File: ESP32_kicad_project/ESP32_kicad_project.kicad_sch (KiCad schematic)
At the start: 24 parts, among them J2 USB_C_Receptacle_USB2.0_16P, J3 Screw_Terminal_01x02, Q1 AO3401A, U1 TPS56339DDC

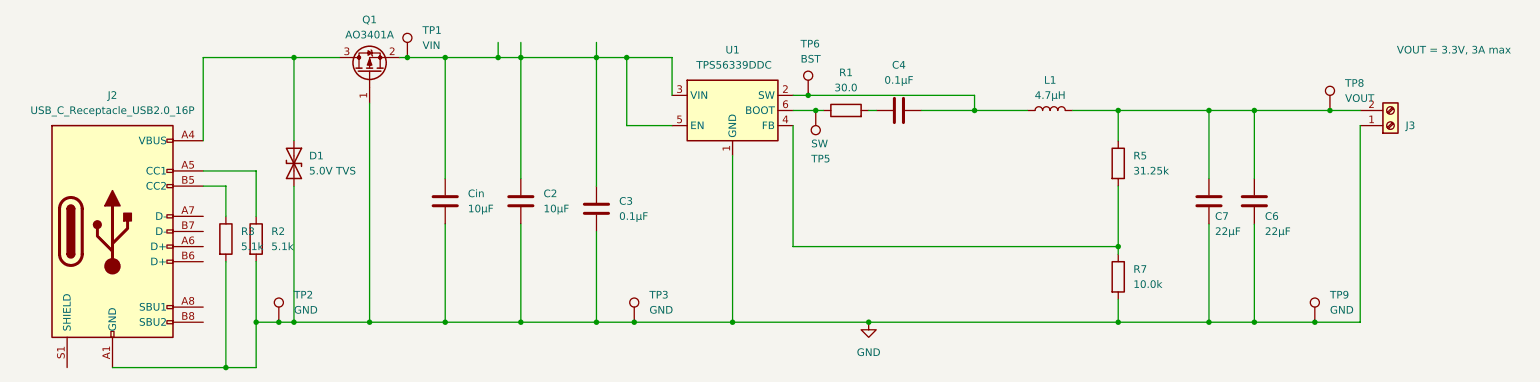
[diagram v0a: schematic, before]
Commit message: added fuse, fixed electrical rules checker errors
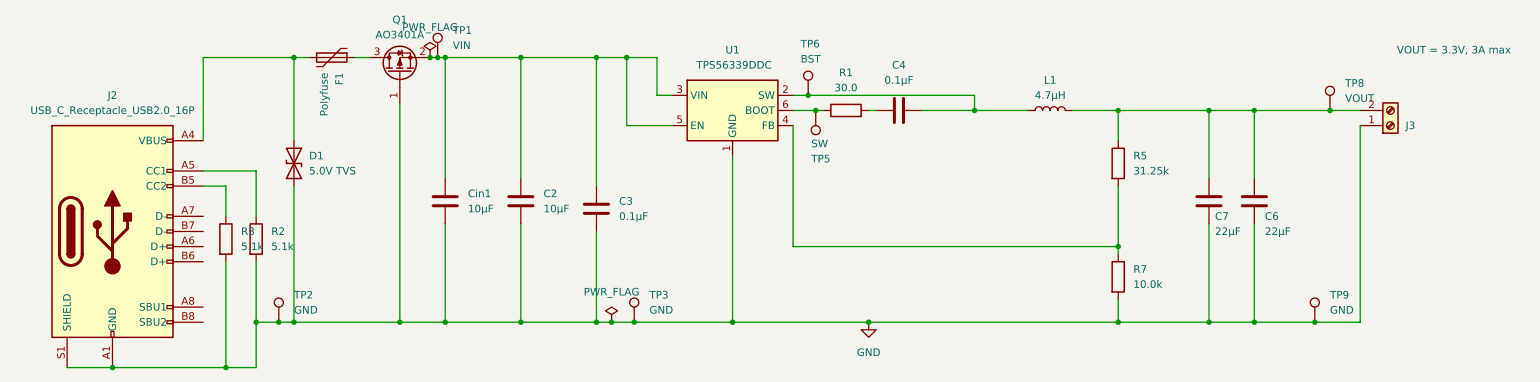
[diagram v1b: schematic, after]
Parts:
- added F1: Polyfuse, Fuse:Fuse_1206_3216Metric, symbol Device:Polyfuse
- D1: footprint Package_TO_SOT_SMD:SOD-323 -> Diode_SMD:D_SOD-323
- renumbered Cin to Cin1
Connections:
- net GND: now also J2.S1 (SHIELD)
- net at D1.1 (A1), J2.A4 (VBUS), J2.A9 (VBUS)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: now also F1.2; no longer Q1.3 (D)
- new net: F1.1, Q1.3 (D)
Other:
- moved on the sheet: Q1, TP1

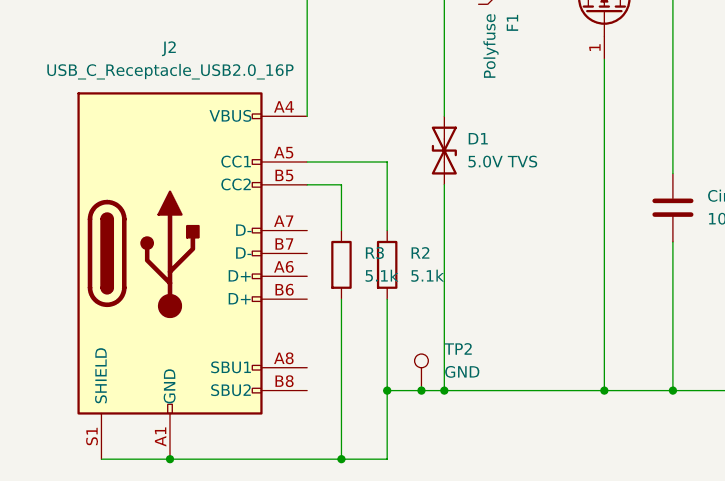
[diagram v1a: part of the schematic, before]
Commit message: created: inductor footprint, assigned it to L1, power unit
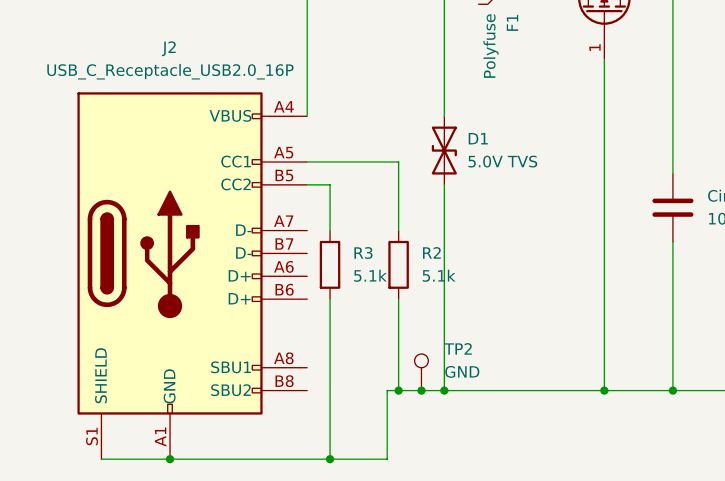
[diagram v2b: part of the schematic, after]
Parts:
- C2, Cin1: footprint (none) -> Capacitor_SMD:C_0805_2012Metric
- C3, C4: footprint (none) -> Capacitor_SMD:C_0603_1608Metric
- C6, C7: footprint (none) -> Capacitor_SMD:C_1206_3216Metric
- D1: footprint Diode_SMD:D_SOD-323 -> Diode_SMD:D_SOD-123
- J2: footprint (none) -> Connector_USB:USB_C_Receptacle_GCT_USB4110
- L1: footprint (none) -> personal_library:Inductor_SDS74M-4R7M-LF
- R1, R5, R7: footprint (none) -> Resistor_SMD:R_0603_1608Metric
- TP1, TP2, TP3, TP5, TP6, TP8, TP9: footprint (none) -> TestPoint:TestPoint_Pad_D1.5mm
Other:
- moved on the sheet: R2, R3
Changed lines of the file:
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@@
-	)
-	(junction
-		(at 67.31 118.11)
-		(diameter 0)
-		(color 0 0 0 0)
 	)
 	(junction
@@
 	)
 	(junction
+		(at 68.58 118.11)
+		(diameter 0)
+		(color 0 0 0 0)
+	)
+	(junction
 		(at 160.02 80.01)
+		(diameter 0)
+		(color 0 0 0 0)
+	)
+	(junction
+		(at 60.96 125.73)
 		(diameter 0)
 		(color 0 0 0 0)
@@
 	)
 	(junction
-		(at 62.23 125.73)
-		(diameter 0)
-		(color 0 0 0 0)
-	)
-	(junction
 		(at 161.29 82.55)
 		(diameter 0)
@@
 	(wire
 		(pts
-			(xy 67.31 118.11) (xy 71.12 118.11)
+			(xy 67.31 118.11) (xy 68.58 118.11)
 		)
 		(stroke
@@
 	(wire
 		(pts
-			(xy 62.23 107.95) (xy 62.23 125.73)
+			(xy 60.96 107.95) (xy 60.96 125.73)
 		)
 		(stroke
@@
 	(wire
 		(pts
-			(xy 58.42 95.25) (xy 62.23 95.25)
+			(xy 58.42 95.25) (xy 60.96 95.25)
 		)
 		(stroke
@@
 	(wire
 		(pts
+			(xy 68.58 118.11) (xy 71.12 118.11)
+		)
+		(stroke
+			(width 0)
+			(type default)
+		)
+	)
+	(wire
+		(pts
 			(xy 147.32 90.17) (xy 147.32 118.11)
 		)
@@
 	(wire
 		(pts
-			(xy 58.42 92.71) (xy 67.31 92.71)
+			(xy 58.42 92.71) (xy 68.58 92.71)
 		)
 		(stroke
@@
 	(wire
 		(pts
+			(xy 60.96 125.73) (xy 67.31 125.73)
+		)
+		(stroke
+			(width 0)
+			(type default)
+		)
+	)
+	(wire
+		(pts
 			(xy 111.76 73.66) (xy 111.76 93.98)
 		)
@@
 	(wire
 		(pts
-			(xy 67.31 92.71) (xy 67.31 100.33)
+			(xy 68.58 92.71) (xy 68.58 100.33)
 		)
 		(stroke
@@
 	(wire
 		(pts
-			(xy 62.23 95.25) (xy 62.23 100.33)
+			(xy 60.96 95.25) (xy 60.96 100.33)
 		)
 		(stroke
@@
 	(wire
 		(pts
-			(xy 43.18 125.73) (xy 62.23 125.73)
+			(xy 43.18 125.73) (xy 60.96 125.73)
 		)
 		(stroke
@@
 	(wire
 		(pts
-			(xy 62.23 125.73) (xy 67.31 125.73)
-		)
-		(stroke
-			(width 0)
-			(type default)
-		)
-	)
-	(wire
-		(pts
 			(xy 67.31 125.73) (xy 67.31 118.11)
 		)
@@
 	(wire
 		(pts
-			(xy 67.31 107.95) (xy 67.31 118.11)
+			(xy 68.58 107.95) (xy 68.58 118.11)
 		)
 		(stroke
@@
 			)
 		)
-		(property "Footprint" ""
+		(property "Footprint" "Capacitor_SMD:C_0603_1608Metric"
 			(at 179.07 81.5848 0)
 			(effects
@@
 			)
 		)
-		(property "Footprint" ""
+		(property "Footprint" "Capacitor_SMD:C_0805_2012Metric"
 			(at 100.0252 101.6 0)
 			(effects
@@
 			)
 		)
-		(property "Footprint" ""
+		(property "Footprint" "TestPoint:TestPoint_Pad_D1.5mm"
 			(at 252.73 82.55 0)
 			(effects
@@
 			)
 		)
-		(property "Footprint" ""
+		(property "Footprint" "Capacitor_SMD:C_1206_3216Metric"
 			(at 228.2952 101.6 0)
 			(effects
@@
 			)
 		)
-		(property "Footprint" ""
+		(property "Footprint" "TestPoint:TestPoint_Pad_D1.5mm"
 			(at 135.89 118.11 0)
 			(effects
@@
 			)
 		)
-		(property "Footprint" ""
+		(property "Footprint" "TestPoint:TestPoint_Pad_D1.5mm"
 			(at 102.87 73.66 0)
 			(effects
@@
 			)
 		)
-		(property "Footprint" ""
+		(property "Footprint" "Resistor_SMD:R_0603_1608Metric"
 			(at 210.312 110.49 90)
 			(effects
@@
 			)
 		)
-		(property "Footprint" ""
+		(property "Footprint" "TestPoint:TestPoint_Pad_D1.5mm"
 			(at 165.1 80.01 0)
 			(effects
@@
 			)
 		)
-		(property "Footprint" ""
+		(property "Footprint" "Capacitor_SMD:C_0603_1608Metric"
 			(at 125.4252 102.87 0)
 			(effects
@@
 			)
 		)
-		(property "Footprint" "Diode_SMD:D_SOD-323"
+		(property "Footprint" "Diode_SMD:D_SOD-123"
 			(at 73.66 91.44 0)
 			(effects
@@
 	(symbol
 		(lib_id "Device:R")
-		(at 67.31 104.14 0)
+		(at 68.58 104.14 0)
 		(unit 1)
 		(exclude_from_sim no)
@@
 		(fields_autoplaced yes)
 		(property "Reference" "R2"
-			(at 69.85 102.8699 0)
+			(at 71.12 102.8699 0)
 			(effects
 				(font
@@
 		)
 		(property "Value" "5.1k"
-			(at 69.85 105.4099 0)
+			(at 71.12 105.4099 0)
 			(effects
 				(font
@@
 		)
 		(property "Footprint" ""
-			(at 65.532 104.14 90)
+			(at 66.802 104.14 90)
 			(effects
 				(font
@@
 		)
 		(property "Datasheet" "~"
-			(at 67.31 104.14 0)
+			(at 68.58 104.14 0)
 			(effects
 				(font
@@
 		)
 		(property "Description" "Resistor"
-			(at 67.31 104.14 0)
+			(at 68.58 104.14 0)
 			(effects
 				(font
@@
 			)
 		)
-		(property "Footprint" ""
+		(property "Footprint" "Capacitor_SMD:C_1206_3216Metric"
 			(at 235.9152 101.6 0)
 			(effects
@@
 			)
 		)
-		(property "Footprint" ""
+		(property "Footprint" "personal_library:Inductor_SDS74M-4R7M-LF"
 			(at 200.66 82.55 0)
 			(effects
@@
 			)
 		)
-		(property "Footprint" ""
+		(property "Footprint" "Capacitor_SMD:C_0805_2012Metric"
 			(at 112.7252 101.6 0)
 			(effects
@@
 			)
 		)
-		(property "Footprint" ""
+		(property "Footprint" "TestPoint:TestPoint_Pad_D1.5mm"
 			(at 76.2 118.11 0)
 			(effects
@@
 			)
 		)
-		(property "Footprint" ""
+		(property "Footprint" "TestPoint:TestPoint_Pad_D1.5mm"
 			(at 166.37 82.55 0)
 			(effects
@@
 			)
 		)
-		(property "Footprint" ""
+		(property "Footprint" "Resistor_SMD:R_0603_1608Metric"
 			(at 166.37 84.328 90)
 			(effects
@@
 			)
 		)
-		(property "Footprint" ""
+		(property "Footprint" "Resistor_SMD:R_0603_1608Metric"
 			(at 210.312 91.44 90)
 			(effects
@@
 	(symbol
 		(lib_id "Device:R")
-		(at 62.23 104.14 0)
+		(at 60.96 104.14 0)
 		(unit 1)
 		(exclude_from_sim no)
@@
 		(fields_autoplaced yes)
 		(property "Reference" "R3"
-			(at 64.77 102.8699 0)
+			(at 63.5 102.8699 0)
 			(effects
 				(font
@@
 		)
 		(property "Value" "5.1k"
-			(at 64.77 105.4099 0)
+			(at 63.5 105.4099 0)
 			(effects
 				(font
@@
 		)
 		(property "Footprint" ""
-			(at 60.452 104.14 90)
+			(at 59.182 104.14 90)
 			(effects
 				(font
@@
 		)
 		(property "Datasheet" "~"
-			(at 62.23 104.14 0)
+			(at 60.96 104.14 0)
 			(effects
 				(font
@@
 		)
 		(property "Description" "Resistor"
-			(at 62.23 104.14 0)
+			(at 60.96 104.14 0)
 			(effects
 				(font
@@
 			)
 		)
-		(property "Footprint" ""
+		(property "Footprint" "TestPoint:TestPoint_Pad_D1.5mm"
 			(at 250.19 118.11 0)
 			(effects
@@
 			)
 		)
-		(property "Footprint" ""
+		(property "Footprint" "Connector_USB:USB_C_Receptacle_GCT_USB4110"
 			(at 46.99 102.87 0)
 			(effects
